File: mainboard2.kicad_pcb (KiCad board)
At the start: 2 copper layers, 80 x 145 mm, 167 parts, among them IC1 AZ1117CH-3.3TRG1, IC10 DRV8873HPWPRQ1, IC11 DRV8873HPWPRQ1, IC2 TC74HC08APF, IC3 AP7375-50SA-7, IC4 NJM78L12SU3-TE1, IC5 MLX91220KDC-ABR-050-SP, IC6 DRV8873HPWPRQ1, IC7 DRV8873HPWPRQ1, IC8 DRV8873HPWPRQ1, IC9 DRV8873HPWPRQ1, J1 Conn_01x03_Socket, J10 Conn_01x03_Socket, J11 Conn_01x02_Socket, J12 Conn_01x02_Socket, J13 Conn_01x04_Socket, J14 Conn_01x02_Socket, J15 Conn_01x02_Socket, J16 Conn_01x02_Socket, J17 Conn_01x02_Socket, J18 Conn_01x02_Socket, J19 Conn_01x02_Socket, J2 Conn_01x03_Socket, J20 Conn_01x02_Socket, J21 USB_C_Receptacle_USB2.0, J3 GPIO, J4 Conn_01x03_Socket, J5 Conn_01x03_Socket, J6 Conn_01x03_Socket, J7 Conn_01x03_Socket, J8 Conn_01x02_Socket, J9 Conn_01x03_Socket, Q1 IRFML8244TRPBF, Q2 IRFML8244TRPBF, Q3 IRFML8244TRPBF, Q4 TPH4R10ANL, Q5 TPH4R10ANL, Q6 IRFML8244TRPBF, Q7 IRFML8244TRPBF, Q8 IRFML8244TRPBF, SW1 SW_Push_Dual_x2, SW3 SW_Push_Dual_x2, U1 PCA9685PW, U2 PCA9685PW, U3 MCP3208, U5 TLP785, U6 TLP785, U7 MCP251863, U8 ESP32-S3-WROOM-1, X1 CSX-750P

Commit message: コンデンサを追加
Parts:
- removed the R17 at (114.2, 61.5)
- removed the R20 at (112.5, 61.5)
- added C10: C, Capacitor_SMD:CP_Elec_10x10.5, F.Cu at (122.5, 78.0)
- added R25: R, Resistor_SMD:R_0603_1608Metric_Pad0.98x0.95mm_HandSolder, F.Cu at (122.9, 127.2)
- added R26: R, Resistor_SMD:R_0603_1608Metric_Pad0.98x0.95mm_HandSolder, F.Cu at (126.2, 127.2)
- added R54: 330Ω, Resistor_SMD:R_0603_1608Metric, B.Cu at (122.1, 68.6)
- added R55: 10Ω, Resistor_SMD:R_0603_1608Metric, B.Cu at (122.1, 70.4)
- R60: renamed from R21; footprint Resistor_THT:R_Axial_DIN0207_L6.3mm_D2.5mm_P10.16mm_Horizontal -> Resistor_SMD:R_2512_6332Metric; moved to B.Cu
- moved Q8 8.42 mm to (122.4, 73.0)
- moved R60 4.11 mm to (124.5, 77.0)
- moved R6 2.54 mm to (132.6, 85.3)
- moved C15 2.18 mm to (115.8, 84.1)
- moved R5 1.66 mm to (129.5, 84.4)
- moved R57 1.16 mm to (127.1, 72.7)
- moved U2 0.40 mm to (117.5, 67.7)
- moved U4 0.24 mm to (115.8, 129.5)
- moved C11 0.07 mm to (154.7, 81.0)
- renumbered C3 to C1, C19 to C11, C15 to C12, C17 to C13, C18 to C14, C26 to C15, C28 to C17, C27 to C18, C25 to C19, C14 to C2, C29 to C20, C39 to C21, C35 to C22, C37 to C23, C31 to C24, C38 to C25, C33 to C26, C36 to C27, C32 to C28, C30 to C29, C11 to C3, C34 to C30, C24 to C31, C20 to C32, C43 to C33, C22 to C34, C23 to C35, C45 to C36, C21 to C37, C44 to C38, C42 to C39, C12 to C4, C46 to C40, C4 to C41, C2 to C42, C40 to C43, C7 to C44, C10 to C45, C1 to C46, C41 to C47, C13 to C5, C5 to C6, C6 to C7, IC4 to IC1, IC11 to IC10, IC1 to IC11, IC3 to IC2, IC2 to IC3, IC5 to IC4, IC6 to IC5, IC8 to IC6, IC10 to IC7, IC9 to IC8, IC7 to IC9, J14 to J1, J12 to J11, J3 to J12, J11 to J13, J6 to J14, J7 to J15, J4 to J16, J5 to J17, J1 to J18, J2 to J19, J8 to J2, J13 to J20, J17 to J3, J15 to J4, J18 to J5, J19 to J6, J20 to J7, J16 to J8, MH2 to MH1, MH4 to MH3, PS2 to PS1, PS1 to PS2, Q5 to Q1, Q4 to Q2, Q2 to Q4, Q1 to Q5, Q7 to Q6, Q8 to Q7, Q6 to Q8, R9 to R1, R50 to R10, R48 to R11, R46 to R12, R49 to R13, R51 to R14, R47 to R15, R55 to R16, R41 to R17, R53 to R18, R40 to R19, R11 to R2, R54 to R20, R42 to R21, R29 to R22, R32 to R23, R34 to R24, R28 to R27, R31 to R28, R33 to R29, R10 to R3, R5 to R30, R3 to R31, R4 to R32, R52 to R33, R1 to R34, R2 to R35, R8 to R36, R6 to R37, R7 to R38, R56 to R39, R38 to R4, R58 to R40, R57 to R41, R14 to R42, R26 to R43, R25 to R44, R24 to R45, R22 to R46, R30 to R47, R15 to R48, R23 to R49, R45 to R5, R18 to R50, R19 to R51, R35 to R52, R36 to R53, R12 to R56, R16 to R57, R13 to R58, R27 to R59, R43 to R6, R37 to R7, R39 to R8, R44 to R9, SW3 to SW2, U6 to U1, U5 to U2, U4 to U3, U3 to U4, U2 to U5, U7 to U6, U1 to U7
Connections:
- U4 pad 1: Iout -> Net-(U3-CH0)
- U4 pad 2: VREF -> Iout
- U4 pad 3: unconnected-(U3-CH2-Pad3) -> VREF
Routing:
- net Net-(Q6-G): track 13.6 -> 4.79 mm
- net Net-(U3-CH0): track 0.00 -> 6.64 mm
- net Net-(Q6-D): track 2.15 -> 4.83 mm
- net Net-(IC8-IPROPI1): track 4.15 -> 6.80 mm
- net Net-(R14-Pad2): track 22.4 -> 20.1 mm, vias 0 -> 1
- net Net-(IC8-IPROPI2): track 1.96 -> 3.61 mm
- net VREF: track 51.3 -> 49.7 mm
- net SPI1.MOSI: track 14.2 -> 15.7 mm
- net Net-(R17-Pad2): track 7.77 -> 9.25 mm
- net Iout: track 53.5 -> 52.4 mm
- net /385_motor1/VIN: track 122.6 -> 121.7 mm, vias 136 -> 149
- net Net-(PS2-+VOUT): track 26.8 -> 27.4 mm
- net GND: vias 217 -> 187
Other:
- board text added: "10A MotorDrivers"
- board text added: "Servo Motors"
- board text removed: "10A MotorDriver"
- board text removed: "DC-DC converter"

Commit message: 少し変更
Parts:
- moved SW2 1.48 mm to (99.0, 179.3)
- moved R39 1.40 mm to (103.0, 178.1)
- moved R25 0.08 mm to (122.9, 127.3)
- moved R26 0.06 mm to (126.2, 127.3)
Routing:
- net +3.3V: track 183.8 -> 182.3 mm
- net /385_motor1/VIN: track 121.7 -> 122.3 mm
- net GND1: vias 16 -> 116
- net GND: vias 187 -> 188
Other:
- board text removed: "Servo Motor"

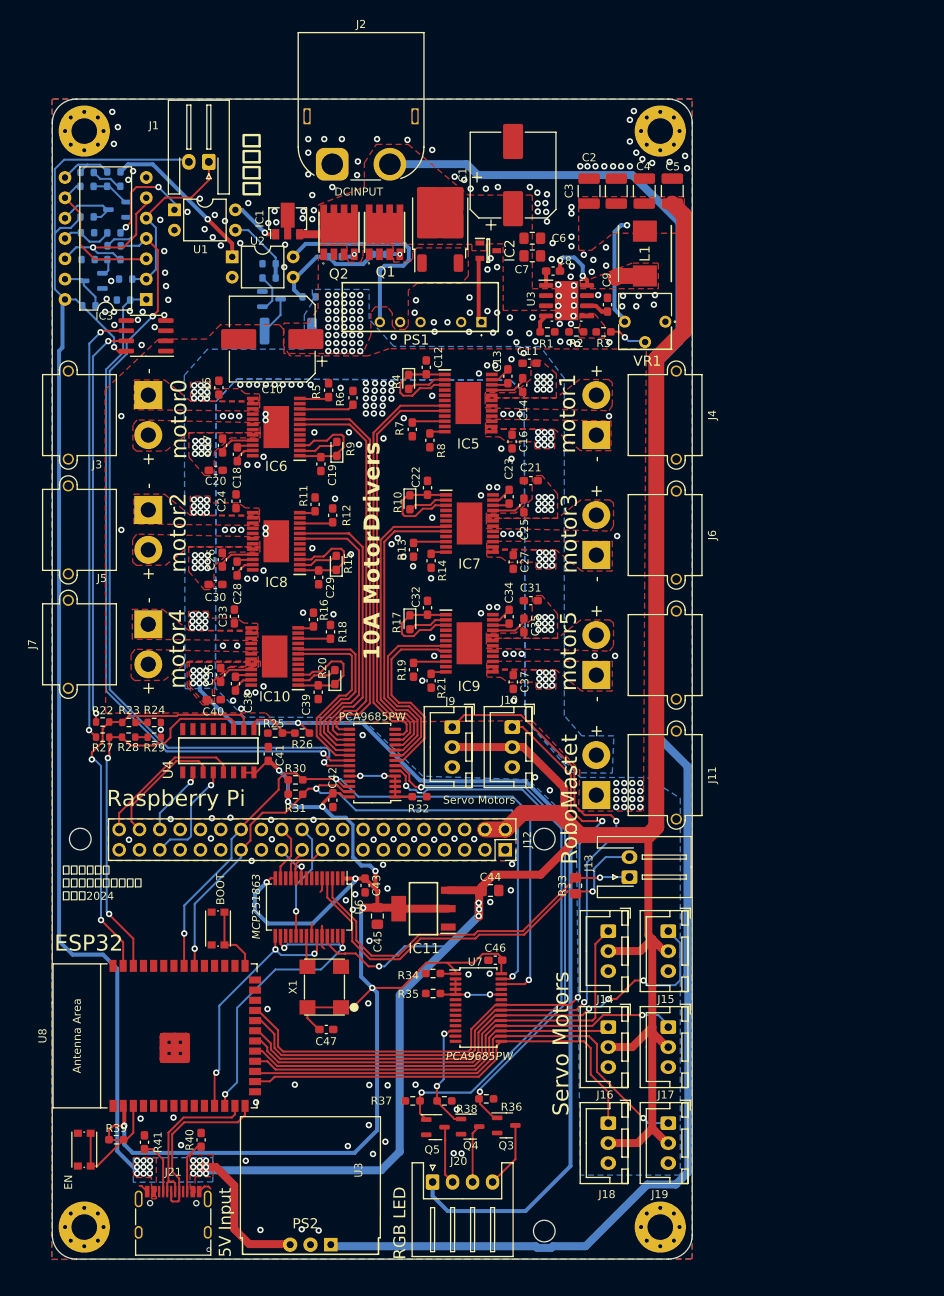
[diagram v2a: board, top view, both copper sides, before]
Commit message: 電流センサー変更
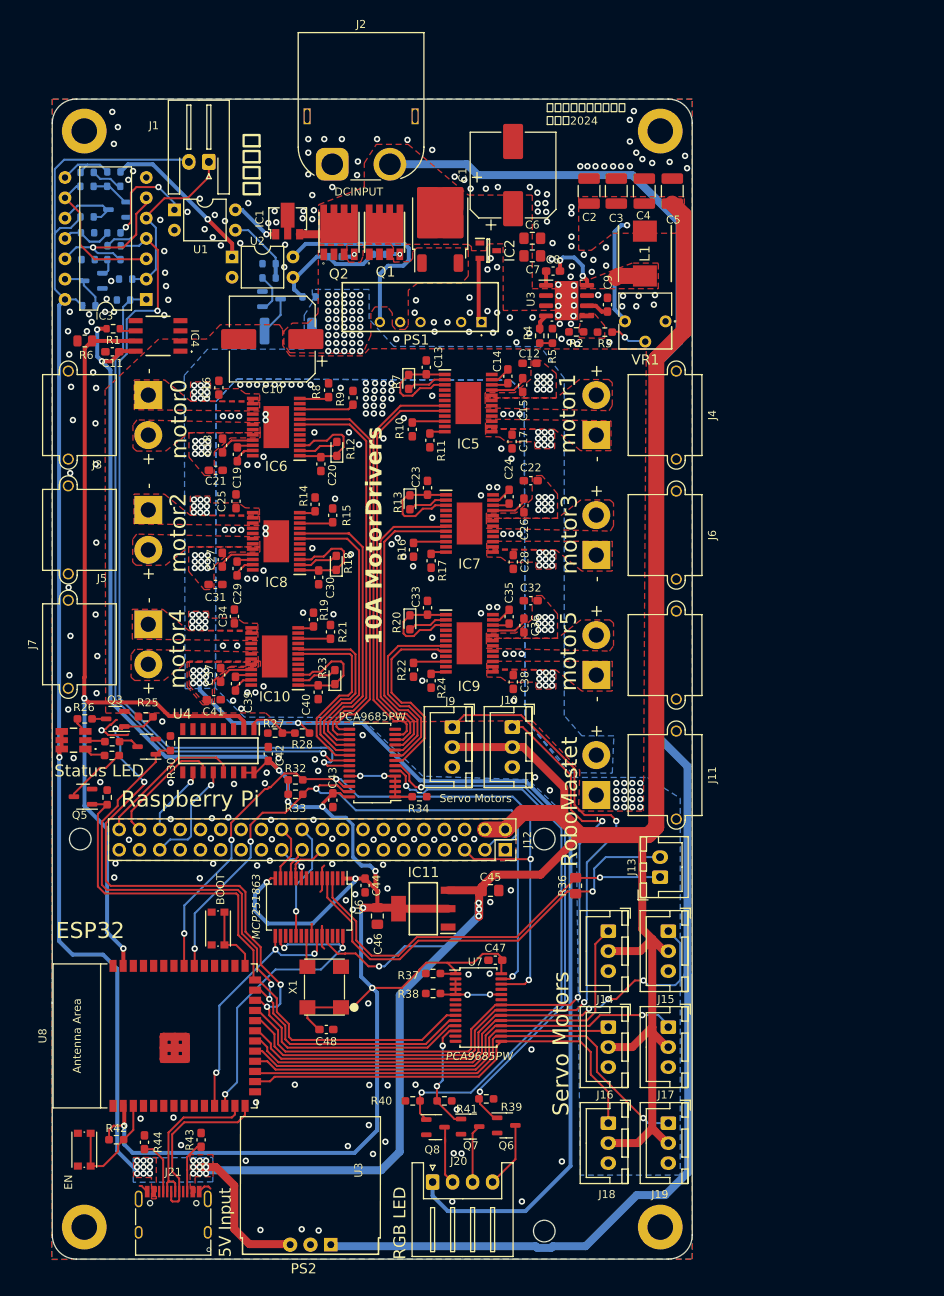
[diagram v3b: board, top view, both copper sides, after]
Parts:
- removed the C44 at (149.8, 146.9)
- removed the R22 at (101.3, 125.9)
- removed the R23 at (104.6, 125.9)
- removed the R24 at (107.7, 125.9)
- removed the R27 at (101.3, 127.8)
- removed the R28 at (104.5, 127.8)
- removed the R54 at (122.1, 68.6)
- removed the R55 at (122.1, 70.4)
- removed REF** (x4): MountingHole_3.2mm_M3_Pad_Via, MountingHole:MountingHole_3.2mm_M3_Pad_Via
- added C11: 0.1μF, Capacitor_SMD:C_0603_1608Metric_Pad1.08x0.95mm_HandSolder, F.Cu at (102.5, 79.6)
- added C46: 10µF, Capacitor_SMD:C_0805_2012Metric_Pad1.18x1.45mm_HandSolder, F.Cu at (135.6, 150.1)
- added H1: MountingHole_Pad, MountingHole:MountingHole_3.2mm_M3_DIN965_Pad, F.Cu at (99.0, 52.0)
- added H2: MountingHole_Pad, MountingHole:MountingHole_3.2mm_M3_DIN965_Pad, F.Cu at (171.0, 52.0)
- added H3: MountingHole_Pad, MountingHole:MountingHole_3.2mm_M3_DIN965_Pad, F.Cu at (99.0, 189.0)
- added H4: MountingHole_Pad, MountingHole:MountingHole_3.2mm_M3_DIN965_Pad, F.Cu at (171.0, 189.0)
- added LED1: NSSM065T, Library:NSSM065T, F.Cu at (97.7, 128.1)
- added Q3: IRFML8244TRPBF, Package_TO_SOT_SMD:SOT-23-3, F.Cu at (102.9, 125.5)
- added Q4: IRFML8244TRPBF, Package_TO_SOT_SMD:SOT-23-3, F.Cu at (106.8, 128.9)
- added Q5: IRFML8244TRPBF, Package_TO_SOT_SMD:SOT-23-3, F.Cu at (98.8, 135.2)
- added R25: R, Resistor_SMD:R_0603_1608Metric_Pad0.98x0.95mm_HandSolder, F.Cu at (106.7, 125.2)
- added R26: R, Resistor_SMD:R_0603_1608Metric_Pad0.98x0.95mm_HandSolder, F.Cu at (99.1, 125.5)
- added R30: R, Resistor_SMD:R_0603_1608Metric_Pad0.98x0.95mm_HandSolder, F.Cu at (109.8, 128.5)
- added R31: R, Resistor_SMD:R_0603_1608Metric_Pad0.98x0.95mm_HandSolder, F.Cu at (102.5, 130.1)
- added R35: R, Resistor_SMD:R_0603_1608Metric_Pad0.98x0.95mm_HandSolder, F.Cu at (101.9, 135.3)
- added R4: 100kΩ, Resistor_SMD:R_0603_1608Metric_Pad0.98x0.95mm_HandSolder, F.Cu at (155.9, 77.6)
- added R5: 100kΩ, Resistor_SMD:R_0603_1608Metric_Pad0.98x0.95mm_HandSolder, F.Cu at (157.5, 77.6)
- added R57: 330Ω, Resistor_SMD:R_0603_1608Metric, B.Cu at (122.1, 68.6)
- added R58: 10Ω, Resistor_SMD:R_0603_1608Metric, B.Cu at (122.1, 70.4)
- added R6: 20kΩ, Resistor_SMD:R_0805_2012Metric, F.Cu at (99.1, 78.2)
- IC4: value MLX91220KDC-ABR-050-SP -> ACS711ELCTR-25AB-T; footprint Package_SO:SOIC-8_3.9x4.9mm_P1.27mm -> Library:ACS711ELCTR-25AB-T
- J13: footprint Connector_JST:JST_XH_S2B-XH-A-1_1x02_P2.50mm_Horizontal -> Connector_JST:JST_XH_B2B-XH-A_1x02_P2.50mm_Vertical
- R1: value R -> 1kΩ; footprint Resistor_SMD:R_0603_1608Metric_Pad0.98x0.95mm_HandSolder -> Resistor_SMD:R_0603_1608Metric
- R29: value 10kΩ -> R; footprint Resistor_SMD:R_0603_1608Metric -> Resistor_SMD:R_0603_1608Metric_Pad0.98x0.95mm_HandSolder
- moved R1 54.3 mm to (102.6, 76.7), turned to 180 degrees
- moved C45 14.5 mm to (149.8, 146.9), turned to 0 degrees
- moved R29 5.28 mm to (102.5, 128.3)
- moved J13 3.82 mm to (171.0, 145.2)
- moved IC4 1.60 mm to (108.3, 77.6), turned to -90 degrees
- moved R3 0.16 mm to (164.1, 77.1)
- moved VR1 0.05 mm to (169.1, 72.2)
- renumbered C11 to C12, C12 to C13, C13 to C14, C14 to C15, C15 to C16, C16 to C17, C17 to C18, C18 to C19, C19 to C20, C20 to C21, C21 to C22, C22 to C23, C23 to C24, C24 to C25, C25 to C26, C26 to C27, C27 to C28, C28 to C29, C29 to C30, C30 to C31, C31 to C32, C32 to C33, C33 to C34, C34 to C35, C35 to C36, C36 to C37, C37 to C38, C38 to C39, C39 to C40, C40 to C41, C41 to C42, C42 to C43, C43 to C44, C46 to C47, C47 to C48, Q7 to Q10, Q8 to Q11, Q3 to Q6, Q4 to Q7, Q5 to Q8, Q6 to Q9, R7 to R10, R8 to R11, R9 to R12, R10 to R13, R11 to R14, R12 to R15, R13 to R16, R14 to R17, R15 to R18, R16 to R19, R17 to R20, R18 to R21, R19 to R22, R20 to R23, R21 to R24, R25 to R27, R26 to R28, R30 to R32, R31 to R33, R32 to R34, R33 to R36, R34 to R37, R35 to R38, R36 to R39, R37 to R40, R38 to R41, R39 to R42, R40 to R43, R41 to R44, R42 to R45, R43 to R46, R44 to R47, R45 to R48, R46 to R49, R47 to R50, R48 to R51, R49 to R52, R50 to R53, R51 to R54, R52 to R55, R53 to R56, R56 to R59, R57 to R60, R58 to R61, R59 to R62, R60 to R63, R4 to R7, R5 to R8, R6 to R9
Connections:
- C45 pad 1: +3.3V -> +5V
- IC4 pad 6: Net-(IC5-VREF) -> /efuse/FAULT
- IC4 pad 7: Net-(IC5-VOUT) -> Iout
- IC4 pad 8: +5V -> +3.3V
- J12 pad 27: SDA -> /ID_SDA
- J12 pad 28: SCL -> /ID_SCL
- J12 pad 3: /GPIO2/SDA1 -> SDA
- J12 pad 5: /GPIO3/SCL1 -> SCL
- R1 pad 1: Net-(U4-RT/CLK) -> /efuse/FAULT
- R1 pad 2: GND -> +3.3V
- R29 pad 1: GND -> Net-(Q4-D)
- U3 pad 4: Net-(U4-RT/CLK) -> Net-(U3-RT/CLK)
- U4 pad 3: VREF -> unconnected-(U4-CH2-Pad3)
- U7 pad 10: unconnected-(U1-LED4-Pad10) -> G_LED
- U7 pad 11: unconnected-(U1-LED5-Pad11) -> B_LED
- U7 pad 9: unconnected-(U1-LED3-Pad9) -> R_LED
- U8 pad 24: unconnected-(U8-GPIO47/SPICLK_P/SUBSPICLK_P_DIFF-Pad24) -> B_LED
- U8 pad 25: unconnected-(U8-GPIO48/SPICLK_N/SUBSPICLK_N_DIFF-Pad25) -> G_LED
- U8 pad 26: unconnected-(U8-GPIO45-Pad26) -> R_LED
- U8 pad 38: VREF -> unconnected-(U8-GPIO2/TOUCH2/ADC1_CH1-Pad38)
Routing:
- net B_LED: track 0.00 -> 93.6 mm, vias 0 -> 4
- net G_LED: track 0.00 -> 84.9 mm, vias 0 -> 2
- net +3.3V: track 182.3 -> 260.4 mm, vias 9 -> 11
- net R_LED: track 0.00 -> 73.4 mm
- net Iout: track 52.3 -> 108.1 mm
- net Net-(IC5-VREF): track 54.9 -> 0.00 mm, vias 2 -> 0
- net Net-(IC5-VOUT): track 51.8 -> 0.00 mm, vias 2 -> 0
- net VREF: track 49.5 -> 0.00 mm, vias 2 -> 0
- net SCL: track 88.7 -> 97.8 mm, vias 3 -> 5
- net Net-(Q5-D): track 0.00 -> 8.06 mm
- net GND: track 35.1 -> 42.7 mm, vias 188 -> 220
- net SDA: track 83.8 -> 88.8 mm, vias 3 -> 4
- net +5V: track 487.9 -> 483.5 mm
- net /Untitled Sheet/CANH: track 52.1 -> 55.4 mm
- net /Untitled Sheet/CANL: track 49.3 -> 52.3 mm
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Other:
- board text added: "Status LED"
- board text added: "ロボコンプロジェクト 制御班2024"
- board text removed: "サレジオ高専 ロボコンプロジェクト 制御班2024"

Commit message: ESP32バージョン
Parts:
- removed C42, C44, C47, C8: 0.1μF, Capacitor_SMD:C_0603_1608Metric_Pad1.08x0.95mm_HandSolder
- removed C48: 100nF, Capacitor_SMD:C_0603_1608Metric_Pad1.08x0.95mm_HandSolder
- removed C5: 47u, Capacitor_SMD:C_1210_3225Metric_Pad1.33x2.70mm_HandSolder
- removed C6, C7: 47u, Capacitor_SMD:C_0805_2012Metric_Pad1.18x1.45mm_HandSolder
- removed C9: 0.01μF, Capacitor_SMD:C_0603_1608Metric_Pad1.08x0.95mm_HandSolder
- removed J21: USB_C_Receptacle_USB2.0, Connector_USB:USB_C_Receptacle_HRO_TYPE-C-31-M-12
- removed L1: CDRH127_LDNP-560MC, Library:INDPM7066X300N
- removed MH1, MH2, MH3: MountingHole_2.7mm_M2.5, MountingHole:MountingHole_2.7mm_M2.5
- removed PS2: BP5293-50, Library:TO254P570X1700X1780-3P
- removed R11, R14, R17, R19, R24: 1.5kΩ, Capacitor_SMD:C_0603_1608Metric_Pad1.08x0.95mm_HandSolder
- removed R32, R33, R37, R38, R42: 10kΩ, Resistor_SMD:R_0603_1608Metric_Pad0.98x0.95mm_HandSolder
- removed R36: 120Ω, Resistor_SMD:R_0805_2012Metric_Pad1.20x1.40mm_HandSolder
- removed R43, R44: 5.1k, Capacitor_SMD:C_0603_1608Metric_Pad1.08x0.95mm_HandSolder
- removed SW2: SW_Push_Dual_x2, Button_Switch_SMD:SW_Push_1P1T_NO_CK_KMR2
- removed U7: PCA9685PW, Package_SO:TSSOP-28_4.4x9.7mm_P0.65mm
- removed U8: ESP32-S3-WROOM-1, PCM_Espressif:ESP32-S3-WROOM-1
- removed VR1: 3362P-1-103LF, Library:3362P_1
- removed X1: CSX-750P, Library:CSX-750P
- added P1: OKLT6W12NC, Library:OKLT6W12NC, F.Cu at (154.2, 65.9)
- C2: value 47u -> 22μF; footprint Capacitor_SMD:C_1210_3225Metric_Pad1.33x2.70mm_HandSolder -> Capacitor_SMD:C_0805_2012Metric_Pad1.18x1.45mm_HandSolder
- C3: value 47u -> 10μF; footprint Capacitor_SMD:C_1210_3225Metric_Pad1.33x2.70mm_HandSolder -> Capacitor_SMD:C_0805_2012Metric_Pad1.18x1.45mm_HandSolder
- C4: value 47u -> 0.1u; footprint Capacitor_SMD:C_1210_3225Metric_Pad1.33x2.70mm_HandSolder -> Capacitor_SMD:C_0603_1608Metric_Pad1.08x0.95mm_HandSolder
- C45, C46, IC11: moved to B.Cu
- J11: value Conn_01x02_Socket -> USB_C_Receptacle_USB2.0; footprint Connector_AMASS:AMASS_XT30PW-M_1x02_P2.50mm_Horizontal -> Connector_USB:USB_C_Receptacle_HCTL_HC-TYPE-C-16P-01A
- J12: value GPIO -> Conn_01x02_Socket; footprint Connector_PinSocket_2.54mm:PinSocket_2x20_P2.54mm_Vertical -> Connector_JST:JST_XH_B2B-XH-A_1x02_P2.50mm_Vertical
- J13: footprint Connector_JST:JST_XH_B2B-XH-A_1x02_P2.50mm_Vertical -> Connector_AMASS:AMASS_XT30PW-F_1x02_P2.50mm_Horizontal
- J20: footprint Connector_JST:JST_XH_S4B-XH-A_1x04_P2.50mm_Horizontal -> Connector_JST:JST_XH_B4B-XH-A_1x04_P2.50mm_Vertical
- J3, J4, J5, J6, J7, J8: footprint Connector_AMASS:AMASS_XT30PW-M_1x02_P2.50mm_Horizontal -> Connector_AMASS:AMASS_XT30PW-F_1x02_P2.50mm_Horizontal
- R2: value R -> 1kΩ; footprint Resistor_SMD:R_0603_1608Metric_Pad0.98x0.95mm_HandSolder -> Resistor_SMD:R_0805_2012Metric_Pad1.20x1.40mm_HandSolder
- R3: value R -> 330Ω; footprint Resistor_SMD:R_0603_1608Metric_Pad0.98x0.95mm_HandSolder -> Resistor_SMD:R_0805_2012Metric_Pad1.20x1.40mm_HandSolder
- R4: value 100kΩ -> 10Ω; footprint Resistor_SMD:R_0603_1608Metric_Pad0.98x0.95mm_HandSolder -> Resistor_SMD:R_0805_2012Metric_Pad1.20x1.40mm_HandSolder
- R5: value 100kΩ -> 10kΩ
- R8: value 1.5kΩ -> 5.1k; footprint Capacitor_SMD:C_0603_1608Metric_Pad1.08x0.95mm_HandSolder -> Resistor_SMD:R_0603_1608Metric_Pad0.98x0.95mm_HandSolder
- U3: value ~ -> ESP32-WROOM-E; footprint Package_SO:SOIC-8-1EP_3.9x4.9mm_P1.27mm_EP2.95x4.9mm_Mask2.71x3.4mm -> PCM_Espressif:ESP32-WROOM-32E
- U4: value MCP3208 -> MCP2562-E-SN; footprint Library:SOIC127P600X175-16N -> Package_SO:SOIC-8_3.9x4.9mm_P1.27mm; moved to B.Cu
- U6: value MCP251863 -> CH330N; footprint Package_SO:SSOP-28_5.3x10.2mm_P0.65mm -> Package_SO:SOIC-8_3.9x4.9mm_P1.27mm; moved to B.Cu
- moved J20 126.4 mm to (161.7, 58.5)
- moved Q8 124.3 mm to (160.3, 53.4)
- moved Q6 123.8 mm to (165.5, 53.3)
- moved LED1 116.2 mm to (185.2, 51.7), turned to 0 degrees
- moved Q7 113.9 mm to (173.0, 65.5)
- moved Q3 108.4 mm to (190.0, 61.0), turned to 0 degrees
- moved Q5 106.0 mm to (187.4, 76.9), turned to 0 degrees
- moved C4 103.1 mm to (116.1, 148.0), turned to 0 degrees
- moved R26 100.6 mm to (182.6, 69.5), turned to 0 degrees
- moved Q4 98.4 mm to (187.4, 72.5), turned to 0 degrees
- moved R35 98.1 mm to (182.6, 79.6), turned to 0 degrees
- moved R29 97.9 mm to (182.6, 72.1), turned to 0 degrees
- moved R31 96.1 mm to (182.6, 77.1), turned to 0 degrees
- moved R25 95.7 mm to (182.6, 67.0)
- moved R30 90.7 mm to (182.6, 74.6), turned to 0 degrees
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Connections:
- C2 pad 1: +5V -> VDD
- C4 pad 1: +5V -> GNDA
- C4 pad 2: GND -> unconnected-(C4-Pad2)
- C45 pad 1: +5V -> Net-(IC11-INPUT)
- IC10 pad 11: unconnected-(IC10-NSLEEP-Pad11) -> Net-(IC10-NFAULT)
- IC10 pad 12: Net-(IC10-IPROPI2) -> Net-(IC10-IPROPI1)
- IC10 pad 9: unconnected-(IC10-DISABLE-Pad9) -> GND1
- IC11 pad 3: +5V -> Net-(IC11-INPUT)
- IC5 pad 11: unconnected-(IC5-NSLEEP-Pad11) -> Net-(IC5-NFAULT)
- IC5 pad 12: Net-(IC5-IPROPI2) -> Net-(IC5-IPROPI1)
- IC5 pad 9: unconnected-(IC5-DISABLE-Pad9) -> GND1
- IC6 pad 11: unconnected-(IC6-NSLEEP-Pad11) -> Net-(IC6-NFAULT)
- IC6 pad 12: Net-(IC6-IPROPI2) -> Net-(IC6-IPROPI1)
- IC6 pad 9: unconnected-(IC6-DISABLE-Pad9) -> GND1
- IC7 pad 11: unconnected-(IC7-NSLEEP-Pad11) -> Net-(IC7-NFAULT)
- IC7 pad 12: Net-(IC7-IPROPI2) -> Net-(IC7-IPROPI1)
- IC7 pad 9: unconnected-(IC7-DISABLE-Pad9) -> GND1
- IC8 pad 11: unconnected-(IC8-NSLEEP-Pad11) -> Net-(IC8-NFAULT)
- IC8 pad 12: Net-(IC8-IPROPI2) -> Net-(IC8-IPROPI1)
- IC8 pad 9: unconnected-(IC8-DISABLE-Pad9) -> GND1
- IC9 pad 11: unconnected-(IC9-NSLEEP-Pad11) -> Net-(IC9-NFAULT)
- IC9 pad 12: Net-(IC9-IPROPI2) -> Net-(IC9-IPROPI1)
- IC9 pad 9: unconnected-(IC9-DISABLE-Pad9) -> GND1
- J12 pad 1: unconnected-(J12-Pin_1-Pad1) -> Net-(J12-Pin_1)
- J12 pad 2: +5V -> Net-(J12-Pin_2)
- J13 pad 1: /Untitled Sheet/CANL -> GND1
- J13 pad 2: /Untitled Sheet/CANH -> unconnected-(J13-Pin_2-Pad2)
- J3 pad 1: Net-(IC6-OUT2_1) -> Net-(IC6-OUT1_1)
- J3 pad 2: Net-(IC6-OUT1_1) -> Net-(IC6-OUT2_1)
- J4 pad 1: Net-(IC5-OUT2_1) -> Net-(IC5-OUT1_1)
- J4 pad 2: Net-(IC5-OUT1_1) -> Net-(IC5-OUT2_1)
- J5 pad 1: Net-(IC8-OUT2_1) -> Net-(IC8-OUT1_1)
- J5 pad 2: Net-(IC8-OUT1_1) -> Net-(IC8-OUT2_1)
- J6 pad 1: Net-(IC7-OUT2_1) -> Net-(IC7-OUT1_1)
- J6 pad 2: Net-(IC7-OUT1_1) -> Net-(IC7-OUT2_1)
- J7 pad 1: Net-(IC10-OUT2_1) -> Net-(IC10-OUT1_1)
- J7 pad 2: Net-(IC10-OUT1_1) -> Net-(IC10-OUT2_1)
- J8 pad 1: Net-(IC9-OUT2_1) -> Net-(IC9-OUT1_1)
- J8 pad 2: Net-(IC9-OUT1_1) -> Net-(IC9-OUT2_1)
- R2 pad 1: Net-(U3-FB) -> Net-(P1-Trim)
- R2 pad 2: GND -> Net-(R2-Pad2)
- R27 pad 1: Net-(U4-CH0) -> Net-(R27-Pad1)
- R28 pad 2: Net-(U4-CH0) -> Net-(R27-Pad1)
- R3 pad 1: Net-(VR1-WIPER) -> Net-(R2-Pad2)
- R3 pad 2: Net-(U3-FB) -> Net-(R3-Pad2)
- R4 pad 1: Net-(U3-RT/CLK) -> Net-(R3-Pad2)
- R4 pad 2: Net-(R4-Pad2) -> GND
- R5 pad 1: Net-(R4-Pad2) -> +3.3V
- R5 pad 2: GND -> Net-(SW1A-D)
- R8 pad 1: Net-(IC6-IPROPI2) -> Net-(J11-CC2)
- R8 pad 2: GND1 -> GNDA
- SW1 pad 1: Net-(SW1A-C) -> GND
- SW1 pad 2: GND -> Net-(SW1A-D)
- U3 pad 1: Net-(U3-BST) -> Net-(U3-GND-Pad1)
- U3 pad 2: VDD -> +3.3V
- U3 pad 3: VDD -> Net-(SW1A-D)
- U3 pad 4: Net-(U3-RT/CLK) -> unconnected-(U3-SENSOR_VP/GPIO36/ADC1_CH0-Pad4)
- U3 pad 5: Net-(U3-FB) -> unconnected-(U3-SENSOR_VN/GPIO39/ADC1_CH3-Pad5)
- U3 pad 6: Net-(U3-SS) -> unconnected-(U3-GPIO34/ADC1_CH6-Pad6)
- U3 pad 7: GND -> unconnected-(U3-GPIO35/ADC1_CH7-Pad7)
- U3 pad 8: Net-(U3-SW) -> unconnected-(U3-32K_XP/GPIO32/ADC1_CH4-Pad8)
- U3 pad 9: GND -> unconnected-(U3-32K_XN/GPIO33/ADC1_CH5-Pad9)
- U4 pad 1: Net-(U4-CH0) -> CANTX
- U4 pad 2: Iout -> GNDA
- U4 pad 3: unconnected-(U4-CH2-Pad3) -> +5V
- U4 pad 4: unconnected-(U4-CH3-Pad4) -> CANRX
- U4 pad 5: unconnected-(U4-CH4-Pad5) -> +3.3V
- U4 pad 6: unconnected-(U4-CH5-Pad6) -> Net-(J12-Pin_2)
- U4 pad 7: unconnected-(U4-CH6-Pad7) -> Net-(J12-Pin_1)
- U4 pad 8: unconnected-(U4-CH7-Pad8) -> GNDA
- U6 pad 1: +3.3V -> Net-(U6-UD+)
- U6 pad 2: unconnected-(U6-NC-Pad2) -> Net-(U6-UD-)
- U6 pad 3: /Untitled Sheet/CANL -> GNDA
- U6 pad 4: /Untitled Sheet/CANH -> unconnected-(U6-~{RTS}-Pad4)
- U6 pad 5: GND -> unconnected-(U6-VCC-Pad5)
- U6 pad 6: unconnected-(U6-nINT1-Pad6) -> UART_TX
- U6 pad 7: unconnected-(U6-nINT0-Pad7) -> UART_RX
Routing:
- net +5V: track 483.5 -> 159.4 mm, vias 24 -> 2
- net +3.3V: track 260.4 -> 9.61 mm, vias 11 -> 2
- net VDD: track 214.8 -> 5.25 mm
- net Iout: track 108.1 -> 5.45 mm, vias 2 -> 0
- net Servo7: track 101.7 -> 0.00 mm, vias 2 -> 0
- net B_LED: track 93.6 -> 0.00 mm, vias 4 -> 0
- net /385_motor1/VIN: track 122.3 -> 32.2 mm, vias 149 -> 148
- net Servo8: track 89.9 -> 0.00 mm, vias 2 -> 0
- net G_LED: track 84.9 -> 0.00 mm, vias 2 -> 0
- net SCL: track 97.8 -> 22.6 mm, vias 5 -> 0
- net R_LED: track 73.4 -> 0.00 mm
- net Servo6: track 67.7 -> 0.00 mm, vias 3 -> 0
- net LED_R: track 67.1 -> 1.18 mm, vias 2 -> 0
- net Servo2: track 61.3 -> 0.00 mm, vias 1 -> 0
- net Servo5: track 58.7 -> 0.00 mm
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- removed copper zone on F.Cu, net +5V
- removed copper zone on B.Cu, net GND1
- removed copper zone on F.Cu, net Net-(U3-FB)
- removed copper zone on F.Cu, net Net-(U3-SW)
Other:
- board size 80 x 145 mm -> 80 x 103 mm
- board text added: "RoboMaster"
- board text removed: "10A MotorDrivers"
- board text removed: "5V Input"
- board text removed: "BOOT"
- board text removed: "DISPLAY (OPTIONAL)"
- board text removed: "EN"
- board text removed: "ESP32"
- board text removed: "PoE"
- board text removed: "RGB LED"
- board text removed: "Raspberry Pi"
- board text removed: "RoboMastet"
- board text removed: "Status LED"
- board text removed: "U3"
